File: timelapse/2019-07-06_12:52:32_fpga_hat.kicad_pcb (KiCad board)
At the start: 4 copper layers, 65 x 56.5 mm, 91 parts, among them J1 2x20, J2 AudioJack3, J3 Conn_02x06_Top_Bottom, J4 Conn_02x06_Top_Bottom, J5 Conn_02x06_Top_Bottom, J6 Conn_01x02, SW1 PTS815, SW2 PTS815, SW3 PTS815, SW4 PTS815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

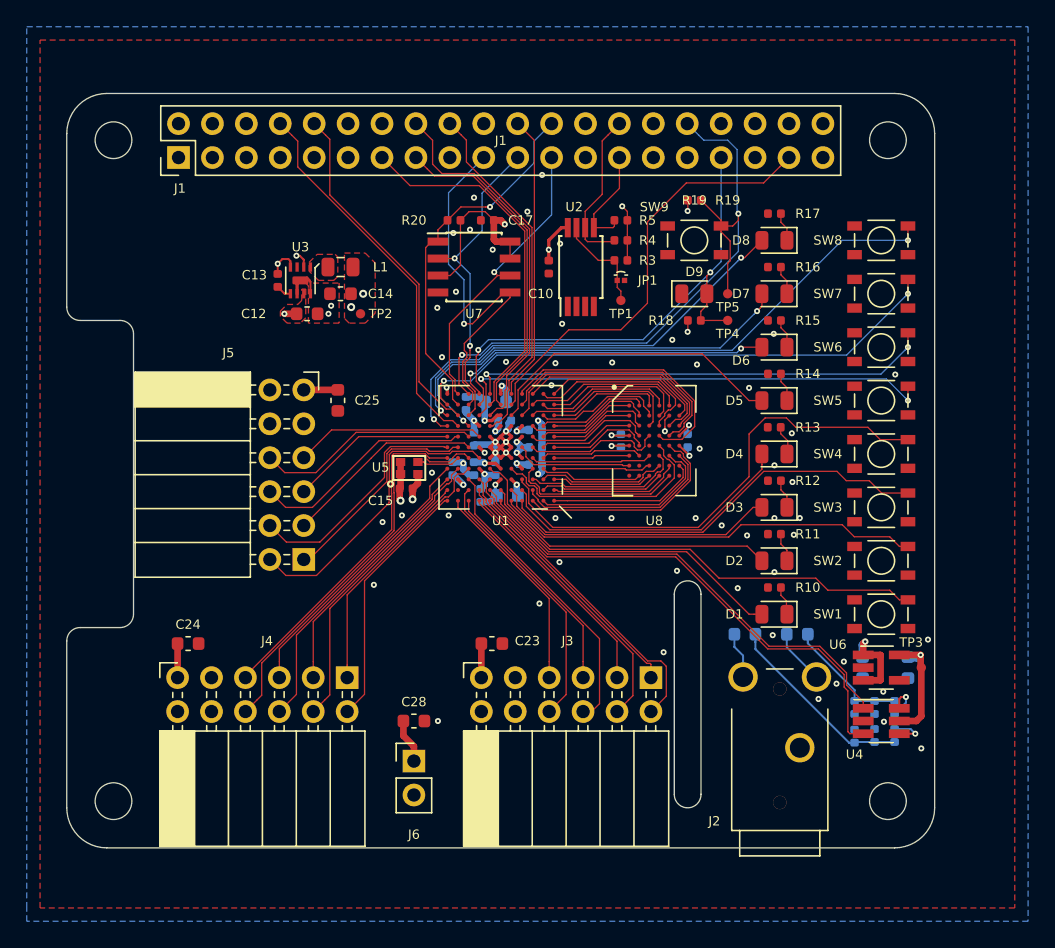
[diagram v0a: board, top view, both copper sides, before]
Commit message: Tidy up L1 silkscreen
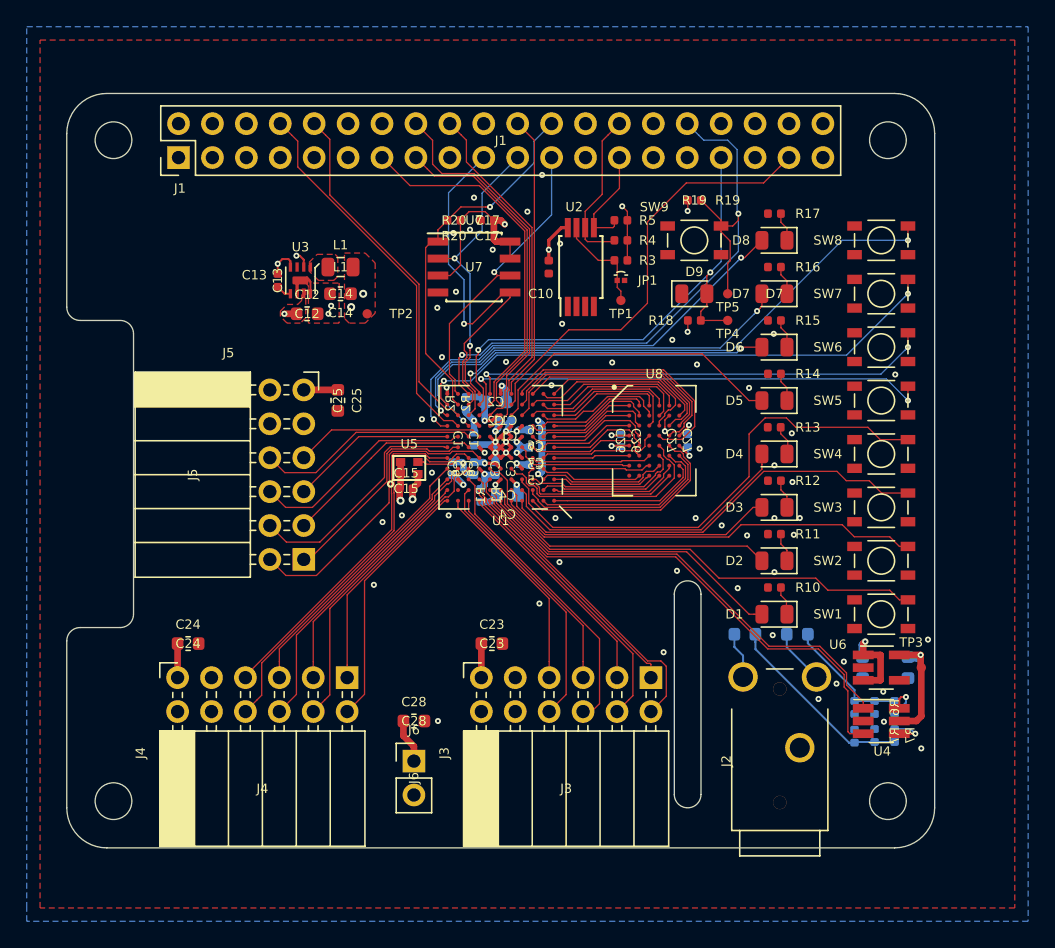
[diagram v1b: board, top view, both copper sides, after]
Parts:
- moved TP2 0.50 mm to (122.5, 96.5)
